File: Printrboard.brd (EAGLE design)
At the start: 100.1 x 63 mm, 127 parts, among them J1 MICROSD, J3 USB-MICRO-PTH, J4 PCIE, Q1 RFP30N06LE, Q2 RFP30N06LE, Q3 RFP30N06LE, U1 LM2841, U10 MCP4728, U2 A4982, U3 A4982, U4 A4982, U5 A4982, U6 AT90USB1286, U7 AP7313, U8 TXB0104, U9 PRTR5V0U4D, X1 16MHz

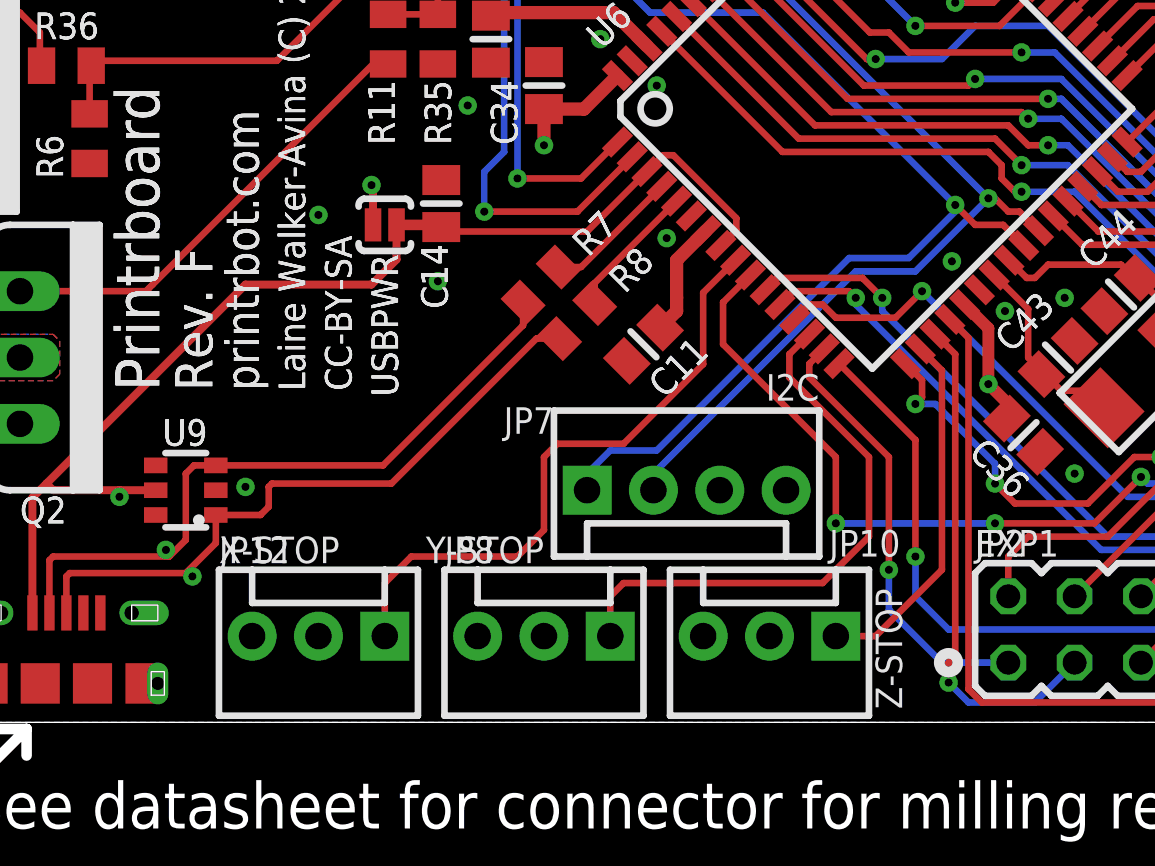
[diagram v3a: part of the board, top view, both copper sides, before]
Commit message: Add in voltage selection and input buffering for the Z-stop
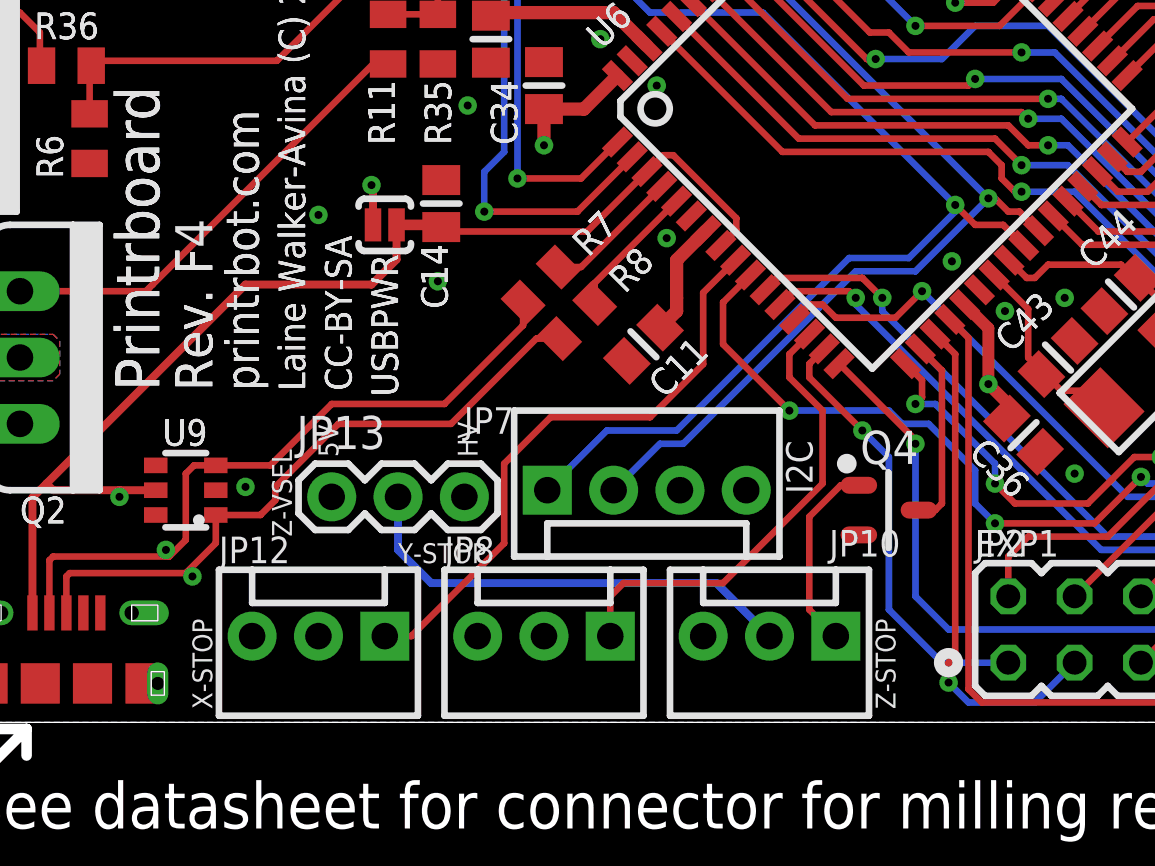
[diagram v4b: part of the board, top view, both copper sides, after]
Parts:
- added JP13: (no value), SparkFun:1X03
- added Q4: RFP30N06LE, ipc-7351-transistor:SOT95P280X135-3N
- moved JP7 1.52 mm to (31.6, 8.89)
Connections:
- new net N$6: JP10.1, Q4.1
- new net N$8: JP10.2, JP13.2
- net +5V: now also JP13.1; no longer JP10.2
- net 12V: now also JP13.3
- net GND: now also Q4.2
- net Z-STOP: now also Q4.3; no longer JP10.1
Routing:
- net 12V: track 47.2 -> 65.1 mm
- net N$8: track 0.00 -> 17.6 mm
- net N$6: track 0.00 -> 7.39 mm
- net Z-STOP: track 13.9 -> 7.25 mm
- net Y-STOP: track 21.7 -> 18.0 mm
- net SDA: track 50.1 -> 51.3 mm
- net SCL: track 49.3 -> 50.4 mm
- net X-STOP: track 23.8 -> 22.8 mm
- net SDCS: track 41.1 -> 40.3 mm
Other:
- board text added: "HV"
- board text added: "Rev. F4"
- board text added: "Z-VSEL"

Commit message: Bump rev to F5 and update copyright date
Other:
- board text added: "Laine Walker-Avina (C) 2015"
- board text added: "Q4"
- board text added: "Rev. F5"
- board text removed: "Rev. F4"
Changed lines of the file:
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@@
 <text x="16.764" y="12.7" size="1.6764" layer="121" ratio="20" rot="R90">Printrboard</text>
 <text x="20.574" y="12.7" size="1.27" layer="121" ratio="20" rot="R90">printrbot.com</text>
-<text x="18.796" y="12.7" size="1.4224" layer="121" ratio="20" rot="R90">Rev. F4</text>
-<text x="22.352" y="12.7" size="1.016" layer="121" ratio="25" rot="R90">Laine Walker-Avina (C) 2013</text>
+<text x="18.796" y="12.7" size="1.4224" layer="121" ratio="20" rot="R90">Rev. F5</text>
+<text x="22.352" y="12.7" size="1.016" layer="121" ratio="25" rot="R90">Laine Walker-Avina (C) 2015</text>
 <text x="88.646" y="13.716" size="1.016" layer="121" ratio="25">Reset</text>
 <text x="24.13" y="12.7" size="1.016" layer="121" ratio="25" rot="R90">CC-BY-SA</text>
@@
 <wire x1="44.6913" y1="9.578009375" x2="44.6913" y2="6.677990625" width="0.254" layer="121"/>
 <circle x="43.091303125" y="9.906990625" radius="0.2499875" width="0.254" layer="121"/>
+<text x="44.958" y="5.334" size="1.016" layer="121" ratio="20">Q4</text>
 </plain>
 <attributes>

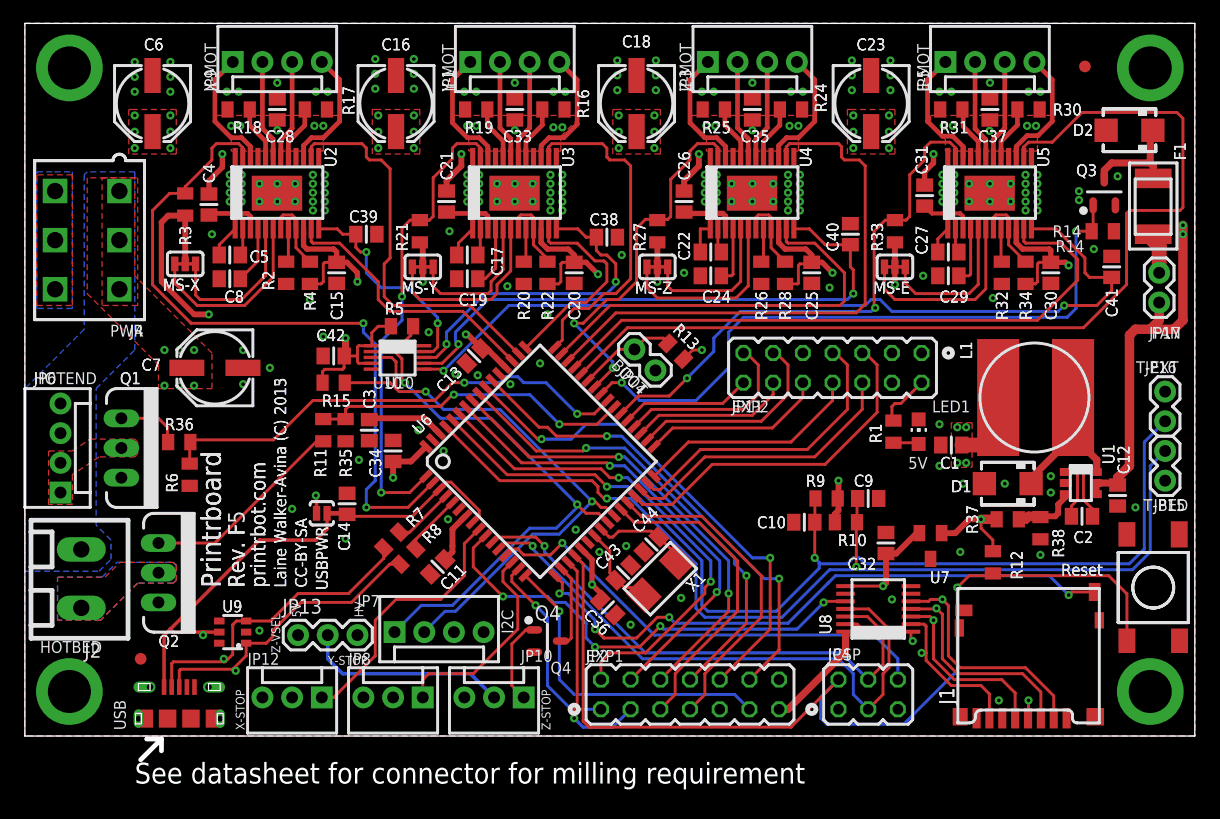
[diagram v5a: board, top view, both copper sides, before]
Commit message: Rev F6
Add second Fan port
Add optional USB-B footprint
Remove polyswitch
Change to push-push microSD socket
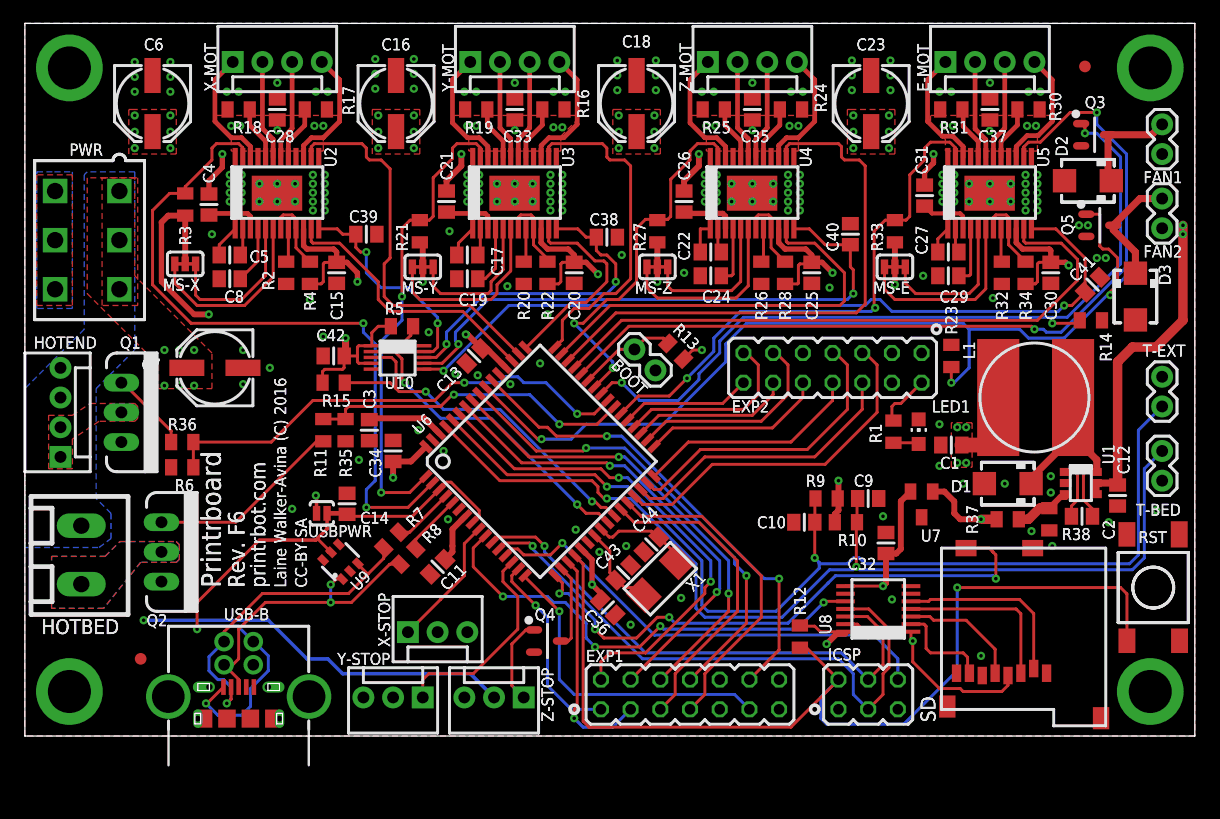
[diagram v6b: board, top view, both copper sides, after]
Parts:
- removed F1: (no value), printrbot:MINISMDC
- removed J1: MICROSD, printrbot:AMPHENOL-MICROSD
- removed J2: (no value), printrbot:PHOENIX-5MM-2POS
- removed J3: USB-MICRO-PTH, printrbot:USB-MICROB-PTH
- removed JP12: X-STOP, SparkFun:MOLEX-1X3
- removed JP13: (no value), SparkFun:1X03
- removed JP15: B-THERM, SparkFun:1X02
- removed JP16: E-THERM, SparkFun:1X02
- removed JP17: FAN, SparkFun:1X02
- removed JP6: HOTEND, SparkFun:MOLEX-1X4
- removed JP7: I2C, SparkFun:MOLEX-1X4
- added D3: (no value), printrbot:SMA
- added FAN1, FAN2: FAN, SparkFun:1X02
- added HOTBED: (no value), printrbot:PHOENIX-5MM-2POS
- added HOTEND: HOTEND, SparkFun:MOLEX-1X4
- added Q5: RFP30N06LE, ipc-7351-transistor:SOT95P280X135-3N
- added R23: 100k, ipc-7351-resistor:RESC2012X70N
- added SD: MICROSD-PP, printrbot:USD-101-00660-68-6
- added T-BED: B-THERM, SparkFun:1X02
- added T-EXT: E-THERM, SparkFun:1X02
- added USB-B: USBPTH, printrbot:USB-B-PTH
- added USB-M: USB-MICRO-PTH, printrbot:USB-MICROB-PTH
- added X-STOP: X-STOP, SparkFun:MOLEX-1X3
- moved R12 17.7 mm to (66.3, 8.51)
- moved U9 11.0 mm to (27.0, 14.9), turned to 45 degrees
- moved R14 7.69 mm to (91.2, 35.6)
- moved D2 5.59 mm to (90.9, 47.5)
- moved Q3 4.96 mm to (91.5, 51.4), turned to 0 degrees
- moved U7 3.64 mm to (76.7, 19.8)
- moved Q1 3.05 mm to (8.26, 27.7)
- moved C41 2.23 mm to (91.3, 38.6), turned to 45 degrees
- moved Q2 1.80 mm to (11.7, 15.7)
- moved R38 1.08 mm to (87.6, 18.5)
- moved R6 0.90 mm to (13.5, 23.0), turned to 180 degrees
- moved R36 0.25 mm to (13.5, 25.1)
- renumbered J4 to PWR, JP1 to Y-MOT, JP10 to Z-STOP, JP11 to EXP2, JP14 to BOOT, JP2 to EXP1, JP3 to Z-MOT, JP4 to ICSP, JP5 to E-MOT, JP8 to Y-STOP, JP9 to X-MOT
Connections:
- removed net N$5: F1.P$1, JP17.2
- removed net TDO: EXP1.10, U6.55
- new net !PWM-FAN2: Q5.1, R23.1, U6.55
- net +3V3: now also SD.P$4; no longer J1.4
- net +5V: now also X-STOP.2; no longer JP12.2, JP13.1, JP7.4
- net 12V: now also FAN1.1, FAN2.1, HOTBED.P$1, HOTEND.3, HOTEND.4, Z-STOP.2; no longer J2.P$1, JP13.3, JP17.1, JP6.3, JP6.4
- net B-THERM: now also T-BED.1; no longer JP15.1
- net E-THERM: now also T-EXT.1; no longer JP16.1
- net GND: now also D3.A, Q5.2, R23.2, SD.GND1, SD.GND2, SD.GND3, SD.P$6, T-BED.2, T-EXT.2, USB-B.GND, USB-M.GND, USB-M.GND1, USB-M.GND2, USB-M.GND3, USB-M.GND4, USB-M.GND5, USB-M.GND6, USB-M.GND7, USB-M.GND8, X-STOP.3; no longer J1.6, J1.C1, J1.C2, J1.C3, J1.C4, J1.CD1, J3.GND, J3.GND1, J3.GND2, J3.GND3, J3.GND4, J3.GND5, J3.GND6, J3.GND7, J3.GND8, JP12.3, JP15.2, JP16.2, JP7.3
- net HOTBED-GND: now also HOTBED.P$2; no longer J2.P$2
- net HOTEND-GND: now also HOTEND.1, HOTEND.2; no longer JP6.1, JP6.2
- net MCU_DN: now also USB-B.D-, USB-M.D-; no longer J3.D-
- net MCU_DP: now also USB-B.D+, USB-M.D+; no longer J3.D+
- net N$2: now also FAN1.2; no longer F1.P$2
- net N$8: now also D3.C, FAN2.2, Q5.3; no longer JP13.2, Z-STOP.2
- net SCL: no longer JP7.1
- net SDA: no longer JP7.2
- net SDCD: now also SD.CD; no longer J1.CD2
- net SDCLK: now also SD.P$5; no longer J1.5
- net SDCSH: now also SD.P$2; no longer J1.2
- net SDDI: now also SD.P$3; no longer J1.3
- net SDDO: now also SD.P$7; no longer J1.7
- net VBUS: now also USB-B.VBUS, USB-M.VBUS; no longer J3.VBUS
- net X-STOP: now also X-STOP.1; no longer JP12.1
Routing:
- net !PWM-FAN2: track 0.00 -> 81.3 mm, vias 0 -> 3
- net TDO: track 44.0 -> 0.00 mm, vias 2 -> 0
- net SCL: track 50.4 -> 30.4 mm
- net SDA: track 51.3 -> 32.3 mm
- net +3V3: track 12.1 -> 25.7 mm, vias 3 -> 2
- net X-STOP: track 22.8 -> 11.3 mm
- net 12V: track 65.1 -> 76.6 mm, vias 56 -> 57
- net !PWM-FAN: track 56.9 -> 68.1 mm, vias 2 -> 3
- net E-DIR: track 84.5 -> 73.5 mm, vias 0 -> 2
- net VBUS: track 44.7 -> 54.6 mm, vias 1 -> 2
- net N$8: track 17.6 -> 10.0 mm
- net SDCLK: track 15.7 -> 10.4 mm, vias 1 -> 0
- net SDDO: track 13.4 -> 8.65 mm, vias 1 -> 0
- net +5V: track 137.4 -> 132.9 mm, vias 20 -> 21
- net VREF_E: track 73.2 -> 68.8 mm
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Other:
- board size 100.1 x 63 mm -> 100.1 x 61 mm
- board text added: "D3"
- board text added: "FAN1"
- board text added: "FAN2"
- board text added: "LED1"
- board text added: "Laine Walker-Avina (C) 2016"
- board text added: "Q5"
- board text added: "R23"
- board text added: "RST"
- board text added: "Rev. F6"
- board text added: "SD"
- board text added: "USB-B"
- board text removed: "/home/ceriand/Downloads/pbrd-logo.bmp"
- board text removed: "5V"
- board text removed: "F1"
- board text removed: "FAN"
- board text removed: "HV"
- board text removed: "I2C"
- board text removed: "J1"
- board text removed: "Laine Walker-Avina (C) 2013"
- board text removed: "Laine Walker-Avina (C) 2015"
- board text removed: "Reset"
- board text removed: "Rev. F"
- board text removed: "Rev. F5"
- board text removed: "See datasheet for connector for milling requirement"
- board text removed: "USB"
- board text removed: "Z-VSEL"

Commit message: Add in changes requested by PBHQ
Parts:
- removed USB-B: USBPTH, printrbot:USB-B-PTH
- moved X-STOP 9.25 mm to (25.4, 3.30), turned to 180 degrees
- moved JP26 7.91 mm to (2.03, 7.37)
- moved USB-M 5.08 mm to (13.2, 2.29)
- moved SD 0.40 mm to (92.9, 16.1)
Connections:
- net GND: no longer USB-B.GND
- net MCU_DN: no longer USB-B.D-
- net MCU_DP: no longer USB-B.D+
- net VBUS: no longer USB-B.VBUS
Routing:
- net VBUS: track 54.6 -> 41.9 mm, vias 2 -> 0
- net X-STOP: track 11.3 -> 21.0 mm
- net MCU_DN: track 27.9 -> 25.8 mm, vias 1 -> 0
- net MCU_DP: track 25.0 -> 26.8 mm
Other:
- board text removed: "USB-B"
